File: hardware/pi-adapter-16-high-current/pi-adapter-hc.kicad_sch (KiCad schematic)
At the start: 34 parts, among them J1 Conn_02x02_Odd_Even, P1 CONN_01X04, P10 CONN_01X04, P11 CONN_01X04, P12 CONN_01X04, P13 CONN_01X04, P14 CONN_01X04, P15 CONN_01X04, P16 CONN_01X04, P17 5V, P2 CONN_01X04, P20 Pi-GPIO, P21 I2C, P22 System SPI, P23 UART, P3 CONN_01X04, P30 +5V, P31 GND, P32 +5V, P4 CONN_01X04, P5 CONN_01X04, P6 CONN_01X04, P7 CONN_01X04, P8 CONN_01X04, P9 CONN_01X04, U1 74HC245, U2 74HC245, U3 74HC245, U4 74HC245

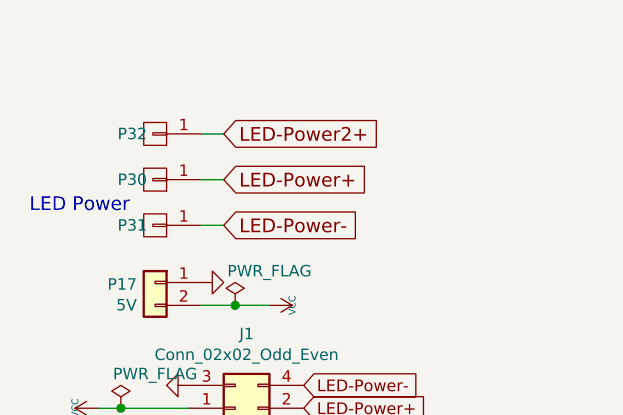
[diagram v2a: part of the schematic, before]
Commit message: Add second LED minus lug for symmetry.
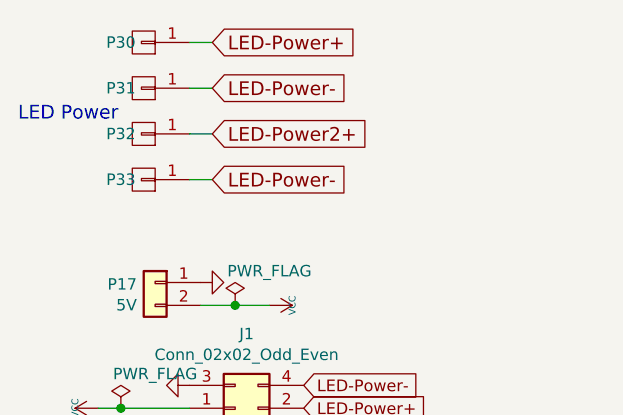
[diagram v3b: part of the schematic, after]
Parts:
- added P33: GND, Connector_PinHeader_1.00mm:PinHeader_1x01_P1.00mm_Vertical, symbol pi-adapter-rescue:CONN_01X01-RESCUE-pi-adapter
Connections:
- net LED-Power-: now also P33.1 (P1)
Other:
- moved on the sheet: P30, P31, P32
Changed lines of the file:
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@@
   (junction (at 147.32 119.38) (diameter 1.016) (color 0 0 0 0))
   (junction (at 147.32 165.1) (diameter 1.016) (color 0 0 0 0))
+  (no_connect (at 48.26 78.74))
+  (no_connect (at 48.26 68.58))
   (no_connect (at 48.26 88.9))
+  (no_connect (at 48.26 101.6))
   (no_connect (at 60.96 101.6))
-  (no_connect (at 48.26 68.58))
-  (no_connect (at 48.26 78.74))
-  (no_connect (at 48.26 101.6))
   (wire (pts (xy 21.59 58.42) (xy 24.13 58.42))
     (stroke (width 0) (type solid) (color 0 0 0 0))
@@
     (stroke (width 0) (type solid) (color 0 0 0 0))
   )
-  (wire (pts (xy 33.02 27.94) (xy 35.56 27.94))
-    (stroke (width 0) (type solid) (color 0 0 0 0))
-  )
-  (wire (pts (xy 33.02 33.02) (xy 35.56 33.02))
-    (stroke (width 0) (type solid) (color 0 0 0 0))
-  )
-  (wire (pts (xy 33.02 38.1) (xy 35.56 38.1))
+  (wire (pts (xy 31.75 17.78) (xy 34.29 17.78))
+    (stroke (width 0) (type solid) (color 0 0 0 0))
+  )
+  (wire (pts (xy 31.75 22.86) (xy 34.29 22.86))
+    (stroke (width 0) (type solid) (color 0 0 0 0))
+  )
+  (wire (pts (xy 31.75 27.94) (xy 34.29 27.94))
+    (stroke (width 0) (type solid) (color 0 0 0 0))
+  )
+  (wire (pts (xy 31.75 33.02) (xy 34.29 33.02))
     (stroke (width 0) (type solid) (color 0 0 0 0))
   )
@@
     (stroke (width 0) (type solid) (color 0 0 0 0))
   )
-  (text "LED Power" (at 13.97 36.83 0)
+  (text "LED Power" (at 12.7 26.67 0)
     (effects (font (size 1.524 1.524)) (justify left bottom))
   )
@@
     (effects (font (size 1.524 1.524)) (justify left bottom))
   )
-  (global_label "LED-Power2+" (shape input) (at 35.56 27.94 0)    (property "Intersheet References" "${INTERSHEET_REFS}" (id 0) (at 56.3953 27.8448 0)
+  (global_label "LED-Power+" (shape input) (at 34.29 17.78 0)    (property "Intersheet References" "${INTERSHEET_REFS}" (id 0) (at -1.27 -15.24 0)
+      (effects (font (size 1.27 1.27)) hide)
+    )
+    (effects (font (size 1.524 1.524)) (justify left))
+  )
+  (global_label "LED-Power-" (shape input) (at 34.29 22.86 0)    (property "Intersheet References" "${INTERSHEET_REFS}" (id 0) (at -1.27 -15.24 0)
+      (effects (font (size 1.27 1.27)) hide)
+    )
+    (effects (font (size 1.524 1.524)) (justify left))
+  )
+  (global_label "LED-Power2+" (shape input) (at 34.29 27.94 0)    (property "Intersheet References" "${INTERSHEET_REFS}" (id 0) (at 55.1253 27.8448 0)
       (effects (font (size 1.524 1.524)) (justify left) hide)
     )
     (effects (font (size 1.524 1.524)) (justify left))
   )
-  (global_label "LED-Power+" (shape input) (at 35.56 33.02 0)    (property "Intersheet References" "${INTERSHEET_REFS}" (id 0) (at 0 0 0)
-      (effects (font (size 1.27 1.27)) hide)
-    )
-    (effects (font (size 1.524 1.524)) (justify left))
-  )
-  (global_label "LED-Power-" (shape input) (at 35.56 38.1 0)    (property "Intersheet References" "${INTERSHEET_REFS}" (id 0) (at 0 0 0)
+  (global_label "LED-Power-" (shape input) (at 34.29 33.02 0)    (property "Intersheet References" "${INTERSHEET_REFS}" (id 0) (at -1.27 -5.08 0)
       (effects (font (size 1.27 1.27)) hide)
     )
@@
     )
   )
-  (symbol (lib_id "pi-adapter-rescue:CONN_01X01-RESCUE-pi-adapter") (at 27.94 27.94 180) (unit 1)
-    (in_bom yes) (on_board yes)
-    (property "Reference" "P32" (id 0) (at 25.4 27.94 0))
-    (property "Value" "+5V" (id 1) (at 25.4 27.94 90)
-      (effects (font (size 1.27 1.27)) hide)
-    )
-    (property "Footprint" "Connector_PinHeader_1.00mm:PinHeader_1x01_P1.00mm_Vertical" (id 2) (at 27.94 27.94 0)
+  (symbol (lib_id "pi-adapter-rescue:CONN_01X01-RESCUE-pi-adapter") (at 26.67 17.78 180) (unit 1)
+    (in_bom yes) (on_board yes)
+    (property "Reference" "P30" (id 0) (at 24.13 17.78 0))
+    (property "Value" "+5V" (id 1) (at 24.13 17.78 90)
+      (effects (font (size 1.27 1.27)) hide)
+    )
+    (property "Footprint" "Connector_PinHeader_1.00mm:PinHeader_1x01_P1.00mm_Vertical" (id 2) (at 26.67 17.78 0)
       (effects (font (size 1.524 1.524)) hide)
     )
-    (property "Datasheet" "" (id 3) (at 27.94 27.94 0)
-      (effects (font (size 1.524 1.524)))
-    )
-  )
-  (symbol (lib_id "pi-adapter-rescue:CONN_01X01-RESCUE-pi-adapter") (at 27.94 33.02 180) (unit 1)
-    (in_bom yes) (on_board yes)
-    (property "Reference" "P30" (id 0) (at 25.4 33.02 0))
-    (property "Value" "+5V" (id 1) (at 25.4 33.02 90)
-      (effects (font (size 1.27 1.27)) hide)
-    )
-    (property "Footprint" "Connector_PinHeader_1.00mm:PinHeader_1x01_P1.00mm_Vertical" (id 2) (at 27.94 33.02 0)
+    (property "Datasheet" "" (id 3) (at 26.67 17.78 0)
+      (effects (font (size 1.524 1.524)))
+    )
+  )
+  (symbol (lib_id "pi-adapter-rescue:CONN_01X01-RESCUE-pi-adapter") (at 26.67 22.86 180) (unit 1)
+    (in_bom yes) (on_board yes)
+    (property "Reference" "P31" (id 0) (at 24.13 22.86 0))
+    (property "Value" "GND" (id 1) (at 24.13 22.86 90)
+      (effects (font (size 1.27 1.27)) hide)
+    )
+    (property "Footprint" "Connector_PinHeader_1.00mm:PinHeader_1x01_P1.00mm_Vertical" (id 2) (at 26.67 22.86 0)
       (effects (font (size 1.524 1.524)) hide)
     )
-    (property "Datasheet" "" (id 3) (at 27.94 33.02 0)
-      (effects (font (size 1.524 1.524)))
-    )
-  )
-  (symbol (lib_id "pi-adapter-rescue:CONN_01X01-RESCUE-pi-adapter") (at 27.94 38.1 180) (unit 1)
-    (in_bom yes) (on_board yes)
-    (property "Reference" "P31" (id 0) (at 25.4 38.1 0))
-    (property "Value" "GND" (id 1) (at 25.4 38.1 90)
-      (effects (font (size 1.27 1.27)) hide)
-    )
-    (property "Footprint" "Connector_PinHeader_1.00mm:PinHeader_1x01_P1.00mm_Vertical" (id 2) (at 27.94 38.1 0)
+    (property "Datasheet" "" (id 3) (at 26.67 22.86 0)
+      (effects (font (size 1.524 1.524)))
+    )
+  )
+  (symbol (lib_id "pi-adapter-rescue:CONN_01X01-RESCUE-pi-adapter") (at 26.67 27.94 180) (unit 1)
+    (in_bom yes) (on_board yes)
+    (property "Reference" "P32" (id 0) (at 24.13 27.94 0))
+    (property "Value" "+5V" (id 1) (at 24.13 27.94 90)
+      (effects (font (size 1.27 1.27)) hide)
+    )
+    (property "Footprint" "Connector_PinHeader_1.00mm:PinHeader_1x01_P1.00mm_Vertical" (id 2) (at 26.67 27.94 0)
       (effects (font (size 1.524 1.524)) hide)
     )
-    (property "Datasheet" "" (id 3) (at 27.94 38.1 0)
+    (property "Datasheet" "" (id 3) (at 26.67 27.94 0)
+      (effects (font (size 1.524 1.524)))
+    )
+  )
+  (symbol (lib_id "pi-adapter-rescue:CONN_01X01-RESCUE-pi-adapter") (at 26.67 33.02 180) (unit 1)
+    (in_bom yes) (on_board yes)
+    (property "Reference" "P33" (id 0) (at 24.13 33.02 0))
+    (property "Value" "GND" (id 1) (at 24.13 33.02 90)
+      (effects (font (size 1.27 1.27)) hide)
+    )
+    (property "Footprint" "Connector_PinHeader_1.00mm:PinHeader_1x01_P1.00mm_Vertical" (id 2) (at 26.67 33.02 0)
+      (effects (font (size 1.524 1.524)) hide)
+    )
+    (property "Datasheet" "" (id 3) (at 26.67 33.02 0)
       (effects (font (size 1.524 1.524)))
     )
@@
       (reference "P32") (unit 1) (value "+5V") (footprint "Connector_PinHeader_1.00mm:PinHeader_1x01_P1.00mm_Vertical")
     )
+    (path "/f640fe79-9dcd-403a-8967-773ea4ffeb8e"
+      (reference "P33") (unit 1) (value "GND") (footprint "Connector_PinHeader_1.00mm:PinHeader_1x01_P1.00mm_Vertical")
+    )
     (path "/112d91ea-543c-4be0-ba81-277d67a718a8"

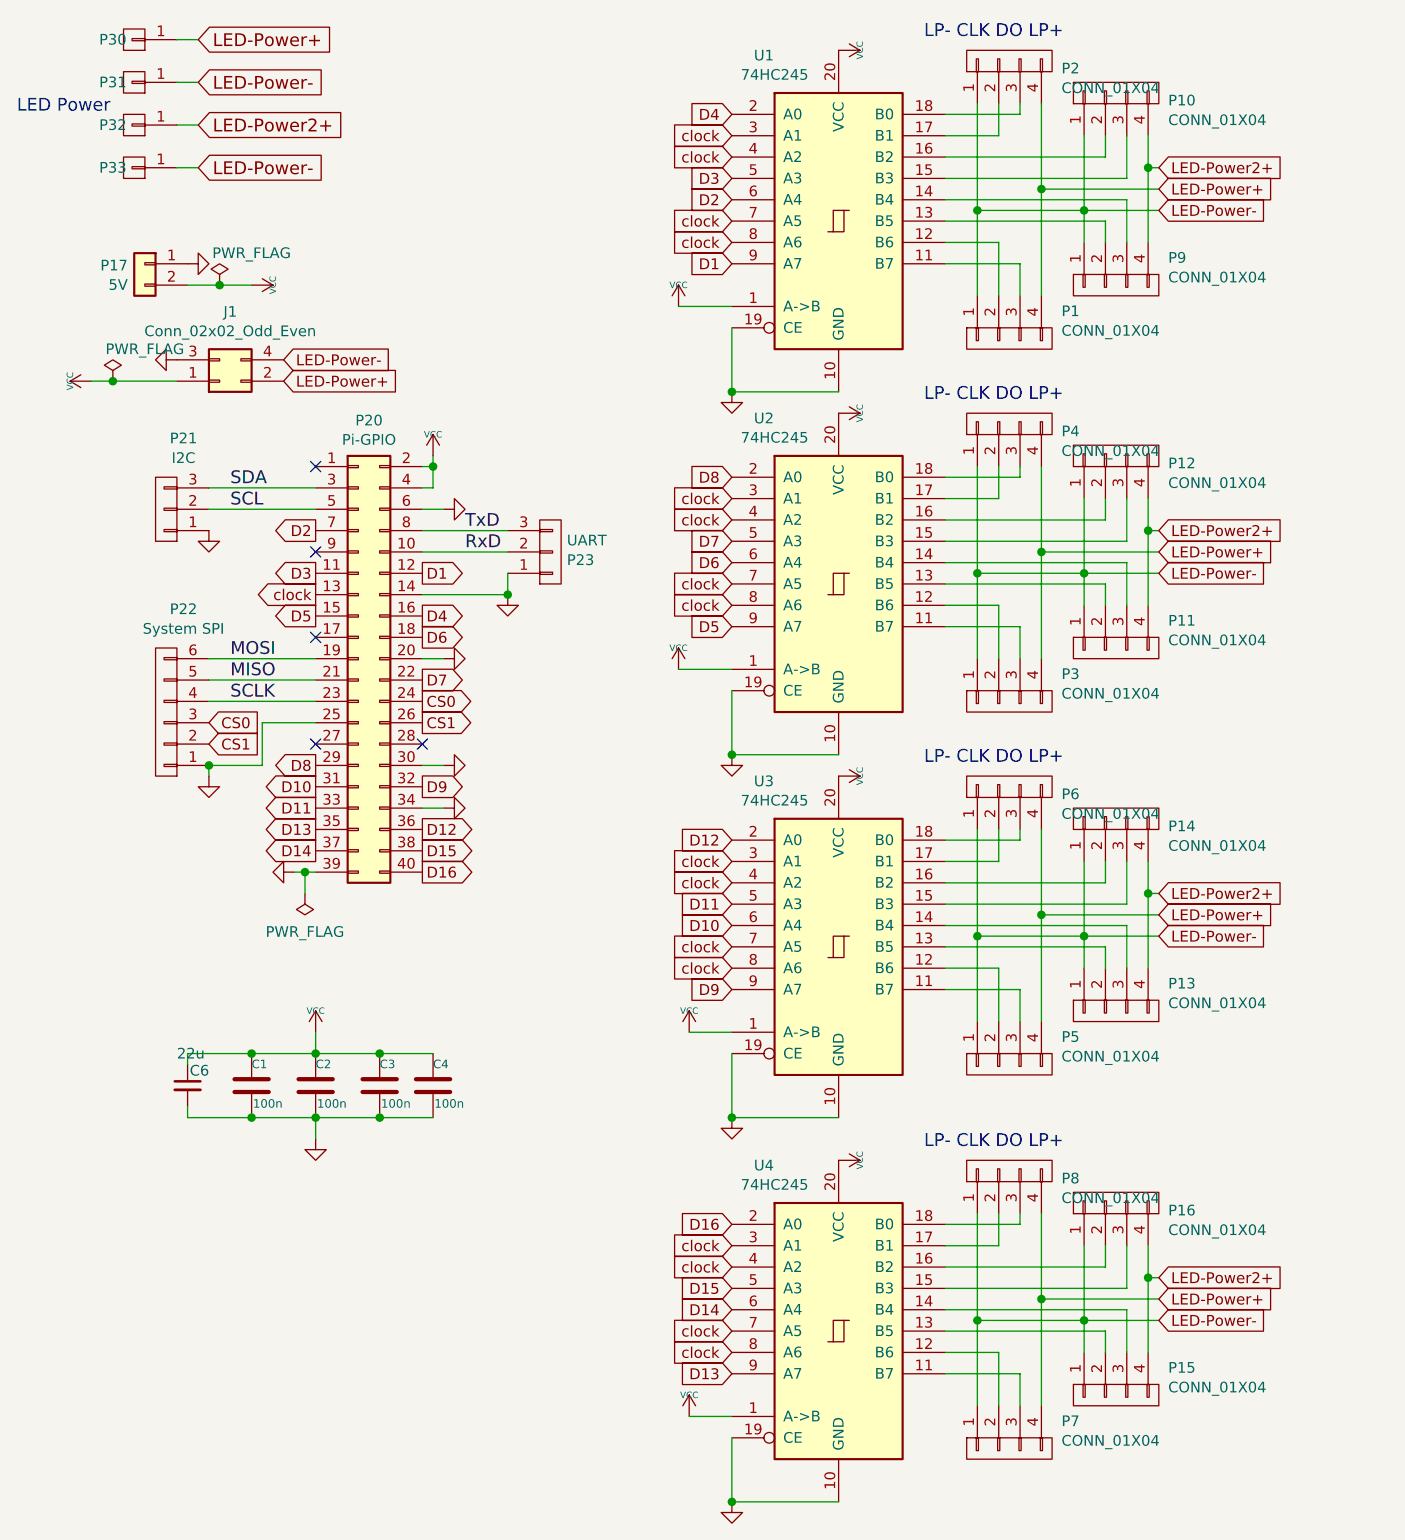
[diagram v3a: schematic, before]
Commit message: Properly mark AHCT245 logic series.
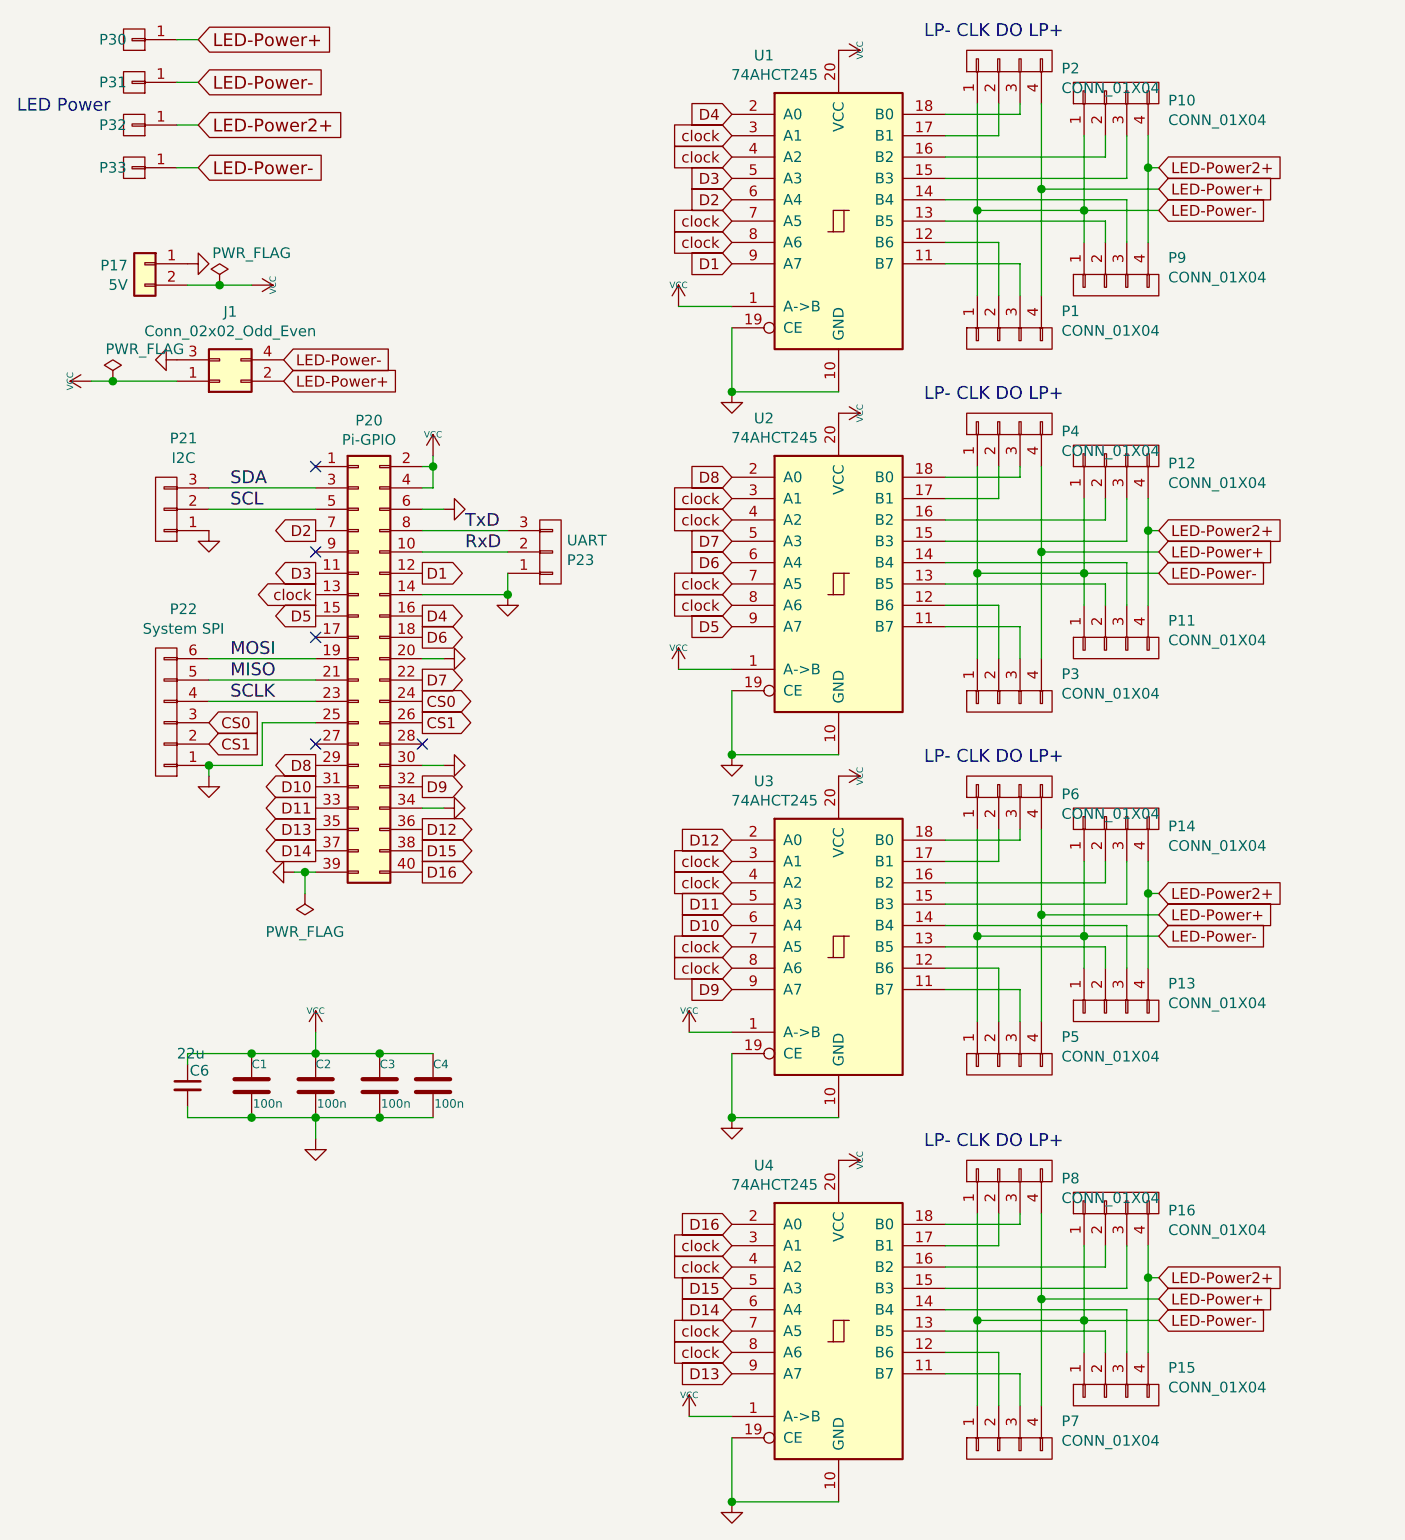
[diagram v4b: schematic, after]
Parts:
- J1, P1, P10, P11, P12, P13, P14, P15, P16, P17, P2, P20, P21, P22, P23, P3, P30, P31, P32, P33, P4, P5, P6, P7, P8, P9: now left out of the parts list
- U1, U2, U3, U4: value 74HC245 -> 74AHCT245
